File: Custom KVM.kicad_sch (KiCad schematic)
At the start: 1 part, among them J1 E9320-001-01

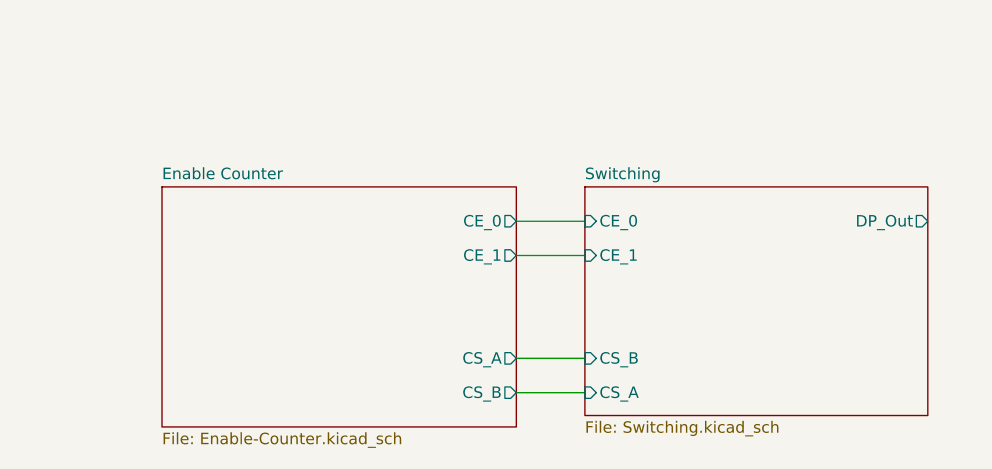
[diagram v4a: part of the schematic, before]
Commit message: Switch debounce, input mDP to switch ICs
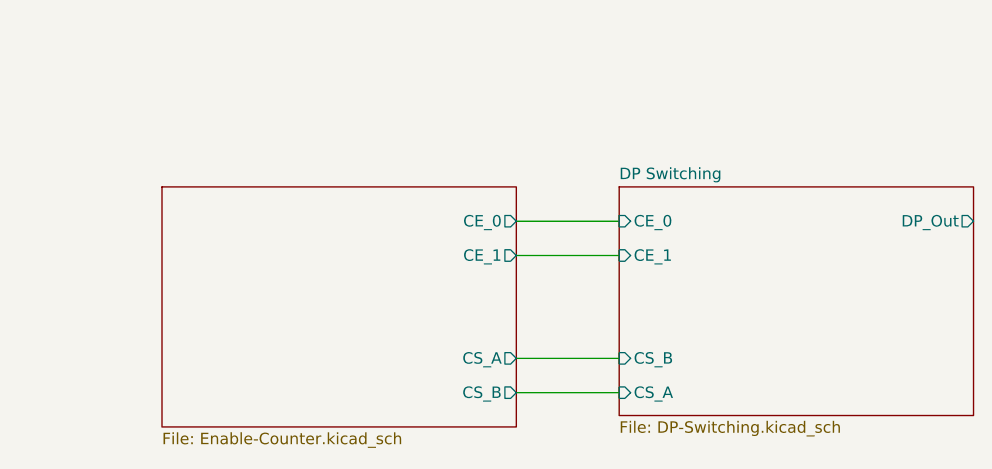
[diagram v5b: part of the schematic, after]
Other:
- sheet Switching renamed DP Switching
- sheet DP Switching: file Switching.kicad_sch -> DP-Switching.kicad_sch
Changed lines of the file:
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@@
-		)
-	)
-	(wire
-		(pts
-			(xy 102.87 160.02) (xy 110.49 160.02)
-		)
-		(stroke
-			(width 0)
-			(type default)
 		)
 	)
@@
 	(wire
 		(pts
+			(xy 102.87 144.78) (xy 114.3 144.78)
+		)
+		(stroke
+			(width 0)
+			(type default)
+		)
+	)
+	(wire
+		(pts
+			(xy 102.87 160.02) (xy 114.3 160.02)
+		)
+		(stroke
+			(width 0)
+			(type default)
+		)
+	)
+	(wire
+		(pts
 			(xy 67.31 46.99) (xy 72.39 46.99)
 		)
@@
 	(wire
 		(pts
-			(xy 102.87 156.21) (xy 110.49 156.21)
-		)
-		(stroke
-			(width 0)
-			(type default)
-		)
-	)
-	(wire
-		(pts
 			(xy 72.39 52.07) (xy 67.31 52.07)
 		)
@@
 		)
 	)
-	(wire
-		(pts
-			(xy 102.87 144.78) (xy 110.49 144.78)
-		)
-		(stroke
-			(width 0)
-			(type default)
-		)
-	)
 	(bus
 		(pts
@@
 	(wire
 		(pts
-			(xy 102.87 140.97) (xy 110.49 140.97)
-		)
-		(stroke
-			(width 0)
-			(type default)
-		)
-	)
-	(wire
-		(pts
 			(xy 67.31 82.55) (xy 67.31 85.09)
 		)
@@
 	(wire
 		(pts
+			(xy 102.87 156.21) (xy 114.3 156.21)
+		)
+		(stroke
+			(width 0)
+			(type default)
+		)
+	)
+	(wire
+		(pts
 			(xy 67.31 90.17) (xy 67.31 92.71)
 		)
@@
 		(pts
 			(xy 67.31 54.61) (xy 72.39 54.61)
+		)
+		(stroke
+			(width 0)
+			(type default)
+		)
+	)
+	(wire
+		(pts
+			(xy 102.87 140.97) (xy 114.3 140.97)
 		)
 		(stroke
@@
 	)
 	(sheet
-		(at 110.49 137.16)
-		(size 38.1 25.4)
+		(at 114.3 137.16)
+		(size 39.37 25.4)
 		(fields_autoplaced yes)
 		(stroke
@@
 			(color 0 0 0 0.0000)
 		)
-		(property "Sheetname" "Switching"
-			(at 110.49 136.4484 0)
+		(property "Sheetname" "DP Switching"
+			(at 114.3 136.4484 0)
 			(effects
 				(font
@@
 			)
 		)
-		(property "Sheetfile" "Switching.kicad_sch"
-			(at 110.49 163.1446 0)
+		(property "Sheetfile" "DP-Switching.kicad_sch"
+			(at 114.3 163.1446 0)
 			(effects
 				(font
@@
 		)
 		(pin "DP_Out" output
-			(at 148.59 140.97 0)
+			(at 153.67 140.97 0)
 			(effects
 				(font
@@
 		)
 		(pin "CE_0" input
-			(at 110.49 140.97 180)
+			(at 114.3 140.97 180)
 			(effects
 				(font
@@
 		)
 		(pin "CE_1" input
-			(at 110.49 144.78 180)
+			(at 114.3 144.78 180)
 			(effects
 				(font
@@
 		)
 		(pin "CS_B" input
-			(at 110.49 156.21 180)
+			(at 114.3 156.21 180)
 			(effects
 				(font
@@
 		)
 		(pin "CS_A" input
-			(at 110.49 160.02 180)
+			(at 114.3 160.02 180)
 			(effects
 				(font
@@
 				)
 				(justify left bottom)
+				(hide yes)
 			)
 		)
@@
 			)
 		)
+		(pin "CE_1" output
+			(at 102.87 144.78 0)
+			(effects
+				(font
+					(size 1.27 1.27)
+				)
+				(justify right)
+			)
+		)
+		(pin "CS_A" output
+			(at 102.87 156.21 0)
+			(effects
+				(font
+					(size 1.27 1.27)
+				)
+				(justify right)
+			)
+		)
+		(pin "CS_B" output
+			(at 102.87 160.02 0)
+			(effects
+				(font
+					(size 1.27 1.27)
+				)
+				(justify right)
+			)
+		)
 		(pin "CE_0" output
 			(at 102.87 140.97 0)
 			(effects
 				(font
-					(size 1.27 1.27)
-				)
-				(justify right)
-			)
-		)
-		(pin "CE_1" output
-			(at 102.87 144.78 0)
-			(effects
-				(font
-					(size 1.27 1.27)
-				)
-				(justify right)
-			)
-		)
-		(pin "CS_A" output
-			(at 102.87 156.21 0)
-			(effects
-				(font
-					(size 1.27 1.27)
-				)
-				(justify right)
-			)
-		)
-		(pin "CS_B" output
-			(at 102.87 160.02 0)
-			(effects
-				(font

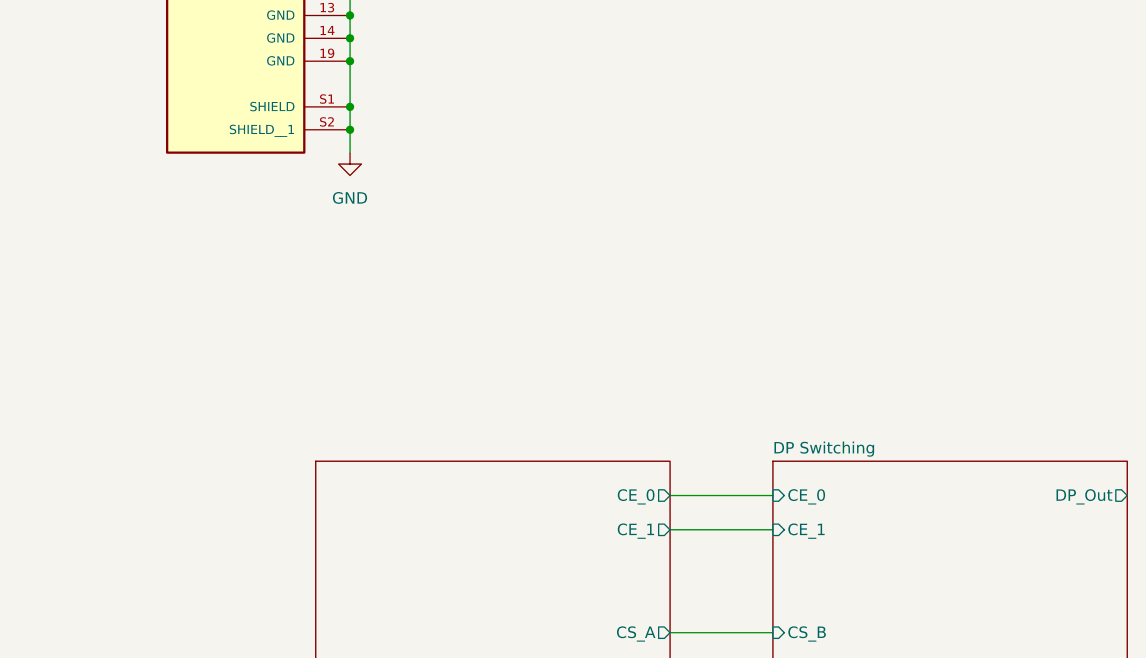
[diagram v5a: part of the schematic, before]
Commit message: Begin USB switching
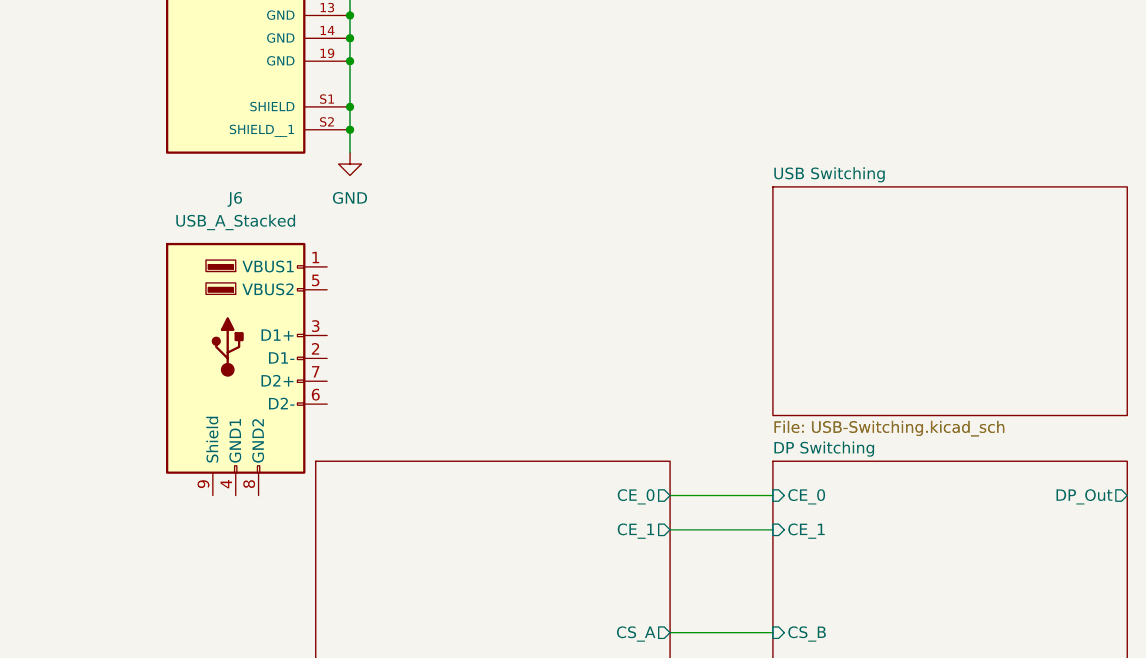
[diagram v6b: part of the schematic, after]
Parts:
- added J6: USB_A_Stacked, symbol Connector:USB_A_Stacked
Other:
- added sheet USB Switching (USB-Switching.kicad_sch)
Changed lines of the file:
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@@
+	)
+	(symbol
+		(lib_id "Connector:USB_A_Stacked")
+		(at 54.61 125.73 0)
+		(unit 1)
+		(exclude_from_sim no)
+		(in_bom yes)
+		(on_board yes)
+		(dnp no)
+		(fields_autoplaced yes)
+		(property "Reference" "J6"
+			(at 54.61 107.95 0)
+			(effects
+				(font
+					(size 1.27 1.27)
+				)
+			)
+		)
+		(property "Value" "USB_A_Stacked"
+			(at 54.61 110.49 0)
+			(effects
+				(font
+					(size 1.27 1.27)
+				)
+			)
+		)
+		(property "Footprint" ""
+			(at 58.42 139.7 0)
+			(effects
+				(font
+					(size 1.27 1.27)
+				)
+				(justify left)
+				(hide yes)
+			)
+		)
+		(property "Datasheet" "~"
+			(at 59.69 124.46 0)
+			(effects
+				(font
+					(size 1.27 1.27)
+				)
+				(hide yes)
+			)
+		)
+		(property "Description" "USB Type A connector, stacked"
+			(at 54.61 125.73 0)
+			(effects
+				(font
+					(size 1.27 1.27)
+				)
+				(hide yes)
+			)
+		)
+		(pin "7"
+		)
+		(pin "4"
+		)
+		(pin "9"
+		)
+		(pin "8"
+		)
+		(pin "6"
+		)
+		(pin "5"
+		)
+		(pin "1"
+		)
+		(pin "3"
+		)
+		(pin "2"
+		)
+		(instances
+			(project "Custom KVM"
+				(path "/0c5b2cf4-6c71-473b-81e1-a704ab2e8eda"
+					(reference "J6")
+					(unit 1)
+				)
+			)
+		)
 	)
 	(symbol
@@
 				)
 			)
+		)
+	)
+	(sheet
+		(at 114.3 106.68)
+		(size 39.37 25.4)
+		(fields_autoplaced yes)
+		(stroke
+			(width 0.1524)
+			(type solid)
+		)
+		(fill
+			(color 0 0 0 0.0000)
+		)
+		(property "Sheetname" "USB Switching"
+			(at 114.3 105.9684 0)
+			(effects
+				(font
+					(size 1.27 1.27)
+				)
+				(justify left bottom)
+			)
+		)
+		(property "Sheetfile" "USB-Switching.kicad_sch"
+			(at 114.3 132.6646 0)
+			(effects
+				(font
+					(size 1.27 1.27)
+				)
+				(justify left top)
+			)
+		)
+		(instances
+			(project "Custom KVM"
+				(path "/0c5b2cf4-6c71-473b-81e1-a704ab2e8eda"
+					(page "4")
+				)
+			)
